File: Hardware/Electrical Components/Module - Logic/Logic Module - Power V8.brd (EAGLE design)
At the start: 72 x 70 mm, 23 parts, among them Q2 130mA/20V

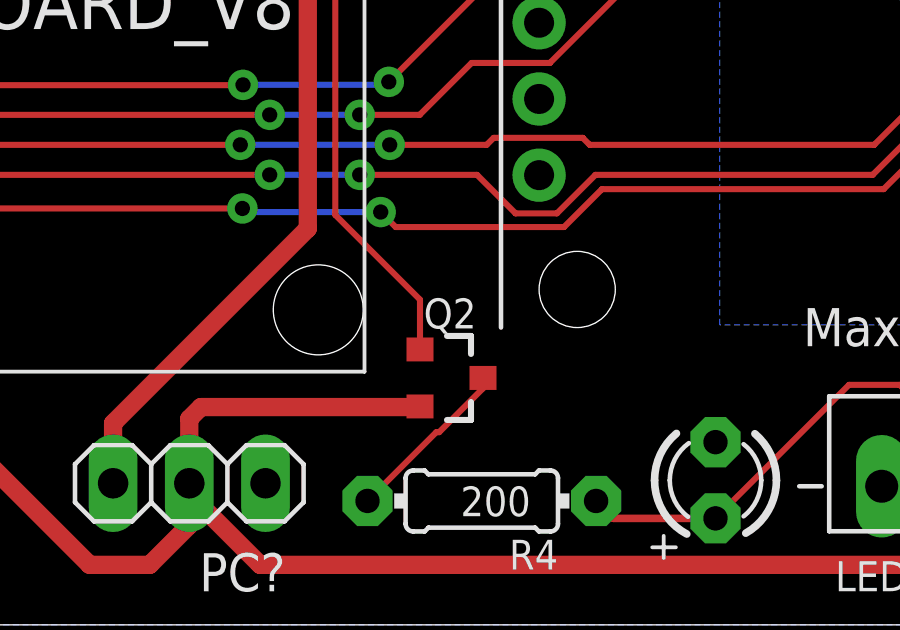
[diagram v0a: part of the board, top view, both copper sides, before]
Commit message: Clarify text in PCBs
O Add text for 3PDT Switch breakout board better PCB annotation
O Rename MOSFET that controls LED for Programming Mode -> P_MOS
+ Add JST Male to BOM Logic Module – Power V8
O Correct excel formula for a total price of Logic Module
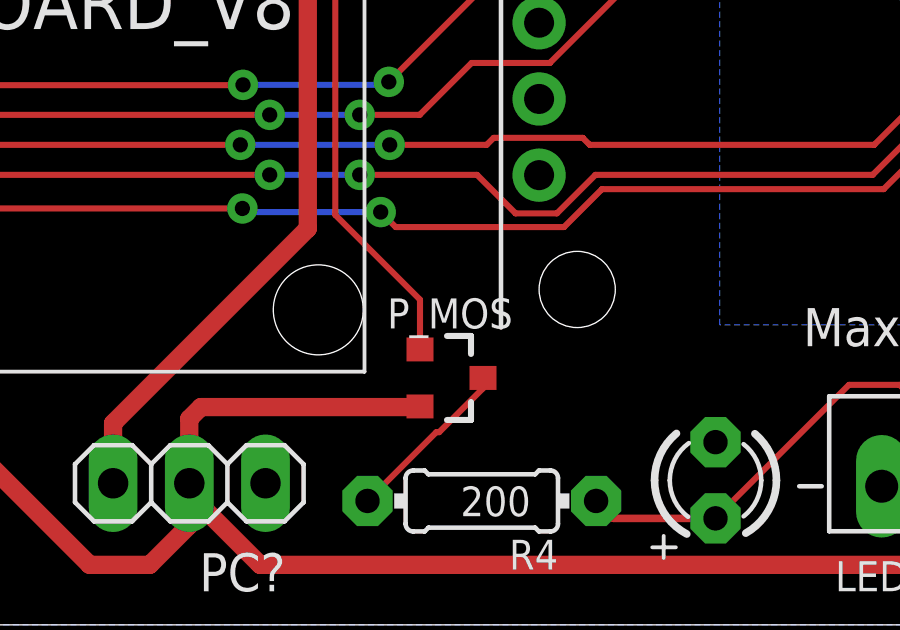
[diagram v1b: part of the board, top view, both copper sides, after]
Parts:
- renumbered Q2 to P_MOS
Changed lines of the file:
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@@
 <attribute name="VALUE" x="65.365" y="26.62" size="1.27" layer="27" rot="R270"/>
 </element>
-<element name="Q2" library="SparkFun-DiscreteSemi" library_urn="urn:adsk.eagle:library:514" package="SOT23-3" package3d_urn="urn:adsk.eagle:package:38446/1" value="130mA/20V" x="38.01" y="8.23" smashed="yes" rot="R270">
+<element name="P_MOS" library="SparkFun-DiscreteSemi" library_urn="urn:adsk.eagle:library:514" package="SOT23-3" package3d_urn="urn:adsk.eagle:package:38446/1" value="130mA/20V" x="38.01" y="8.23" smashed="yes" rot="R270">
 <attribute name="NAME" x="38.01" y="9.881" size="1" layer="25" font="vector" ratio="10" align="bottom-center"/>
 <attribute name="PROD_ID" value="TRANS-11153" x="38.01" y="8.23" size="1.778" layer="27" rot="R270" display="off"/>
@@
 <wire x1="67" y1="2" x2="70.0894" y2="5.0894" width="0.6096" layer="1"/>
 <wire x1="70.0894" y1="23.8006" x2="68.54" y2="25.35" width="0.6096" layer="1"/>
-<contactref element="Q2" pad="2"/>
+<contactref element="P_MOS" pad="2"/>
 <wire x1="29.32" y1="4.72" x2="29.32" y2="6.87" width="0.6096" layer="1"/>
 <wire x1="29.32" y1="6.87" x2="29.71" y2="7.26" width="0.6096" layer="1"/>
@@
 </signal>
 <signal name="WAKE_NOSLEEP">
-<contactref element="Q2" pad="1"/>
+<contactref element="P_MOS" pad="1"/>
 <contactref element="MS1" pad="10"/>
 <wire x1="37.01" y1="9.18" x2="37.01" y2="10.840525" width="0.2032" layer="1"/>
@@
 </signal>
 <signal name="N$2">
-<contactref element="Q2" pad="3"/>
+<contactref element="P_MOS" pad="3"/>
 <contactref element="R4" pad="2"/>
 <wire x1="37.64938125" y1="6.4228" x2="37.5528" y2="6.4228" width="0.2032" layer="1"/>
